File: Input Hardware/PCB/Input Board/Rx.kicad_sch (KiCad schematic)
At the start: 32 parts

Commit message: Update Schematic
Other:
- removed sheet Rx Preamp 5
- removed sheet Rx Preamp 6
- removed sheet Rx Preamp 7
- removed sheet Rx Preamp 8
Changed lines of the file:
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@@
 	)
 	(sheet
-		(at 101.6 73.66)
-		(size 12.7 43.18)
+		(at 203.2 22.86)
+		(size 12.7 93.98)
 		(exclude_from_sim no)
 		(in_bom yes)
@@
 		)
 		(property "Sheetname" "Rx Preamp 4"
-			(at 101.6 72.9484 0)
+			(at 203.2 22.1484 0)
+			(effects
+				(font
+					(size 1.27 1.27)
+				)
+				(justify left bottom)
+			)
+		)
+		(property "Sheetfile" "Rx_Preamp.kicad_sch"
+			(at 203.2 117.4246 0)
+			(effects
+				(font
+					(size 1.27 1.27)
+				)
+				(justify left top)
+			)
+		)
+		(instances
+			(project "Input Board"
+				(path "/198ad8d1-66e3-4deb-889c-1af2b81e67c3/e110e9b7-e557-4981-bab6-c28116ad040e"
+					(page "9")
+				)
+			)
+		)
+	)
+	(sheet
+		(at 152.4 22.86)
+		(size 12.7 93.98)
+		(exclude_from_sim no)
+		(in_bom yes)
+		(on_board yes)
+		(dnp no)
+		(fields_autoplaced yes)
+		(stroke
+			(width 0.1524)
+			(type solid)
+		)
+		(fill
+			(color 0 0 0 0.0000)
+		)
+		(property "Sheetname" "Rx Preamp 3"
+			(at 152.4 22.1484 0)
+			(effects
+				(font
+					(size 1.27 1.27)
+				)
+				(justify left bottom)
+			)
+		)
+		(property "Sheetfile" "Rx_Preamp.kicad_sch"
+			(at 152.4 117.4246 0)
+			(effects
+				(font
+					(size 1.27 1.27)
+				)
+				(justify left top)
+			)
+		)
+		(instances
+			(project "Input Board"
+				(path "/198ad8d1-66e3-4deb-889c-1af2b81e67c3/e110e9b7-e557-4981-bab6-c28116ad040e"
+					(page "7")
+				)
+			)
+		)
+	)
+	(sheet
+		(at 101.6 22.86)
+		(size 12.7 93.98)
+		(exclude_from_sim no)
+		(in_bom yes)
+		(on_board yes)
+		(dnp no)
+		(fields_autoplaced yes)
+		(stroke
+			(width 0.1524)
+			(type solid)
+		)
+		(fill
+			(color 0 0 0 0.0000)
+		)
+		(property "Sheetname" "Rx Preamp 2"
+			(at 101.6 22.1484 0)
 			(effects
 				(font
@@
 			(project "Input Board"
 				(path "/198ad8d1-66e3-4deb-889c-1af2b81e67c3/e110e9b7-e557-4981-bab6-c28116ad040e"
-					(page "6")
-				)
-			)
-		)
-	)
-	(sheet
-		(at 203.2 22.86)
-		(size 12.7 43.18)
-		(exclude_from_sim no)
-		(in_bom yes)
-		(on_board yes)
-		(dnp no)
-		(fields_autoplaced yes)
-		(stroke
-			(width 0.1524)
-			(type solid)
-		)
-		(fill
-			(color 0 0 0 0.0000)
-		)
-		(property "Sheetname" "Rx Preamp 7"
-			(at 203.2 22.1484 0)
-			(effects
-				(font
-					(size 1.27 1.27)
-				)
-				(justify left bottom)
-			)
-		)
-		(property "Sheetfile" "Rx_Preamp.kicad_sch"
-			(at 203.2 66.6246 0)
-			(effects
-				(font
-					(size 1.27 1.27)
-				)
-				(justify left top)
-			)
-		)
-		(instances
-			(project "Input Board"
-				(path "/198ad8d1-66e3-4deb-889c-1af2b81e67c3/e110e9b7-e557-4981-bab6-c28116ad040e"
-					(page "9")
-				)
-			)
-		)
-	)
-	(sheet
-		(at 152.4 22.86)
-		(size 12.7 43.18)
-		(exclude_from_sim no)
-		(in_bom yes)
-		(on_board yes)
-		(dnp no)
-		(fields_autoplaced yes)
-		(stroke
-			(width 0.1524)
-			(type solid)
-		)
-		(fill
-			(color 0 0 0 0.0000)
-		)
-		(property "Sheetname" "Rx Preamp 5"
-			(at 152.4 22.1484 0)
-			(effects
-				(font
-					(size 1.27 1.27)
-				)
-				(justify left bottom)
-			)
-		)
-		(property "Sheetfile" "Rx_Preamp.kicad_sch"
-			(at 152.4 66.6246 0)
-			(effects
-				(font
-					(size 1.27 1.27)
-				)
-				(justify left top)
-			)
-		)
-		(instances
-			(project "Input Board"
-				(path "/198ad8d1-66e3-4deb-889c-1af2b81e67c3/e110e9b7-e557-4981-bab6-c28116ad040e"
-					(page "7")
-				)
-			)
-		)
-	)
-	(sheet
-		(at 101.6 22.86)
-		(size 12.7 43.18)
-		(exclude_from_sim no)
-		(in_bom yes)
-		(on_board yes)
-		(dnp no)
-		(fields_autoplaced yes)
-		(stroke
-			(width 0.1524)
-			(type solid)
-		)
-		(fill
-			(color 0 0 0 0.0000)
-		)
-		(property "Sheetname" "Rx Preamp 3"
-			(at 101.6 22.1484 0)
-			(effects
-				(font
-					(size 1.27 1.27)
-				)
-				(justify left bottom)
-			)
-		)
-		(property "Sheetfile" "Rx_Preamp.kicad_sch"
-			(at 101.6 66.6246 0)
-			(effects
-				(font
-					(size 1.27 1.27)
-				)
-				(justify left top)
-			)
-		)
-		(instances
-			(project "Input Board"
-				(path "/198ad8d1-66e3-4deb-889c-1af2b81e67c3/e110e9b7-e557-4981-bab6-c28116ad040e"
 					(page "5")
 				)
@@
 	)
 	(sheet
-		(at 203.2 73.66)
-		(size 12.7 43.18)
-		(exclude_from_sim no)
-		(in_bom yes)
-		(on_board yes)
-		(dnp no)
-		(fields_autoplaced yes)
-		(stroke
-			(width 0.1524)
-			(type solid)
-		)
-		(fill
-			(color 0 0 0 0.0000)
-		)
-		(property "Sheetname" "Rx Preamp 8"
-			(at 203.2 72.9484 0)
-			(effects
-				(font
-					(size 1.27 1.27)
-				)
-				(justify left bottom)
-			)
-		)
-		(property "Sheetfile" "Rx_Preamp.kicad_sch"
-			(at 203.2 117.4246 0)
-			(effects
-				(font
-					(size 1.27 1.27)
-				)
-				(justify left top)
-			)
-		)
-		(instances
-			(project "Input Board"
-				(path "/198ad8d1-66e3-4deb-889c-1af2b81e67c3/e110e9b7-e557-4981-bab6-c28116ad040e"
-					(page "10")
-				)
-			)
-		)
-	)
-	(sheet
-		(at 50.8 73.66)
-		(size 12.7 43.18)
-		(exclude_from_sim no)
-		(in_bom yes)
-		(on_board yes)
-		(dnp no)
-		(fields_autoplaced yes)
-		(stroke
-			(width 0.1524)
-			(type solid)
-		)
-		(fill
-			(color 0 0 0 0.0000)
-		)
-		(property "Sheetname" "Rx Preamp 2"
-			(at 50.8 72.9484 0)
-			(effects
-				(font
-					(size 1.27 1.27)
-				)
-				(justify left bottom)
-			)
-		)
-		(property "Sheetfile" "Rx_Preamp.kicad_sch"
-			(at 50.8 117.4246 0)
-			(effects
-				(font
-					(size 1.27 1.27)
-				)
-				(justify left top)
-			)
-		)
-		(instances
-			(project "Input Board"
-				(path "/198ad8d1-66e3-4deb-889c-1af2b81e67c3/e110e9b7-e557-4981-bab6-c28116ad040e"
-					(page "4")
-				)
-			)
-		)
-	)
-	(sheet
-		(at 152.4 73.66)
-		(size 12.7 43.18)
-		(exclude_from_sim no)
-		(in_bom yes)
-		(on_board yes)
-		(dnp no)
-		(fields_autoplaced yes)
-		(stroke
-			(width 0.1524)
-			(type solid)
-		)
-		(fill
-			(color 0 0 0 0.0000)
-		)
-		(property "Sheetname" "Rx Preamp 6"
-			(at 152.4 72.9484 0)
-			(effects
-				(font
-					(size 1.27 1.27)
-				)
-				(justify left bottom)
-			)
-		)
-		(property "Sheetfile" "Rx_Preamp.kicad_sch"
-			(at 152.4 117.4246 0)
-			(effects
-				(font
-					(size 1.27 1.27)
-				)
-				(justify left top)
-			)
-		)
-		(instances
-			(project "Input Board"
-				(path "/198ad8d1-66e3-4deb-889c-1af2b81e67c3/e110e9b7-e557-4981-bab6-c28116ad040e"
-					(page "8")
-				)
-			)
-		)
-	)
-	(sheet
-		(at 50.8 22.86)
-		(size 12.7 43.18)
+		(at 50.8 24.13)
+		(size 12.7 92.71)
 		(exclude_from_sim no)
 		(in_bom yes)
@@
 		)
 		(property "Sheetname" "Rx Preamp  1"
-			(at 50.8 22.1484 0)
+			(at 50.8 23.4184 0)
 			(effects
 				(font
@@
 		)
 		(property "Sheetfile" "Rx_Preamp.kicad_sch"
-			(at 50.8 66.6246 0)
+			(at 50.8 117.4246 0)
 			(effects
 				(font

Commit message: Fix Name
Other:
- sheet Rx Preamp  1 renamed Rx Preamp 1
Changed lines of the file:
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@@
 			(color 0 0 0 0.0000)
 		)
-		(property "Sheetname" "Rx Preamp  1"
+		(property "Sheetname" "Rx Preamp 1"
 			(at 50.8 23.4184 0)
 			(effects

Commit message: Power Board, Row amplifier setup etc
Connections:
- net Rx Row Amplifier 1/RXIN5: now reaches L205.2
- net Rx Row Amplifier 1/RXIN6: now reaches L206.2
- net Rx Row Amplifier 1/RXIN4: now reaches L204.2
- net Rx Row Amplifier 1/RXIN8: now reaches L208.2
- net Rx Row Amplifier 1/RXIN7: now reaches L207.2
- net Rx Row Amplifier 1/RXIN2: now reaches L202.2
- net Rx Row Amplifier 1/RXIN1: now reaches L201.2
- net Rx Row Amplifier 1/RXIN3: now reaches L203.2
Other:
- sheet Rx Preamp 1 renamed Rx Row Amplifier 1
- sheet Rx Preamp 2 renamed Rx Row Amplifier 2
- sheet Rx Preamp 3 renamed Rx Row Amplifier 3
- sheet Rx Preamp 4 renamed Rx Row Amplifier 4
- sheet Rx Row Amplifier 1 ports: added RXIN1, RXIN2, RXIN3, RXIN4, RXIN5, RXIN6, RXIN7, RXIN8, RXOUT1, RXOUT2, RXOUT3, RXOUT4, RXOUT5, RXOUT6, RXOUT7, RXOUT8; removed none
- moved on the sheet: L201, L202, L203, L204, L205, L206, L207, L208, L209, L210, L211, L212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

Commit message: explosion 💥
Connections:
- net Rx Row Amplifier 4/RXIN4: now reaches L228.2
- net Rx Row Amplifier 2/RXOUT4: now reaches L212.2
- net Rx Row Amplifier 4/RXIN6: now reaches L230.2
- net Rx Row Amplifier 2/RXIN8: now reaches L213.2
- net Rx Row Amplifier 3/RXIN3: now reaches L219.2
- net Rx Row Amplifier 3/RXIN1: now reaches L217.2
- net Rx Row Amplifier 4/RXIN7: now reaches L231.2
- net Rx Row Amplifier 2/RXOUT2: now reaches L210.2
- net Rx Row Amplifier 2/RXIN1: now reaches L209.2
- net Rx Row Amplifier 4/RXIN5: now reaches L229.2
- net Rx Row Amplifier 4/RXIN1: now reaches L225.2
- net Rx Row Amplifier 3/RXIN5: now reaches L221.2
- net Rx Row Amplifier 3/RXIN7: now reaches L223.2
- net Rx Row Amplifier 4/RXIN3: now reaches L227.2
- net Rx Row Amplifier 4/RXIN8: now reaches L232.2
- net Rx Row Amplifier 3/RXOUT4: now reaches L220.2
- net Rx Row Amplifier 2/RXIN7: now reaches L214.2
- net Rx Row Amplifier 2/RXOUT7: now reaches L216.2
- net Rx Row Amplifier 3/RXIN6: now reaches L222.2
- net Rx Row Amplifier 3/RXOUT2: now reaches L218.2
- net Rx Row Amplifier 3/RXIN8: now reaches L224.2
- net Rx Row Amplifier 2/RXIN5: now reaches L215.2
- net Rx Row Amplifier 2/RXIN3: now reaches L211.2
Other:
- sheet Rx Row Amplifier 2 ports: added RXIN1, RXIN2, RXIN3, RXIN4, RXIN5, RXIN6, RXIN7, RXIN8, RXOUT1, RXOUT2, RXOUT3, RXOUT4, RXOUT5, RXOUT6, RXOUT7, RXOUT8; removed none
- sheet Rx Row Amplifier 3 ports: added RXIN1, RXIN2, RXIN3, RXIN4, RXIN5, RXIN6, RXIN7, RXIN8, RXOUT1, RXOUT2, RXOUT3, RXOUT4, RXOUT5, RXOUT6, RXOUT7, RXOUT8; removed none
- sheet Rx Row Amplifier 4 ports: added RXIN1, RXIN2, RXIN3, RXIN4, RXIN5, RXIN6, RXIN7, RXIN8, RXOUT1, RXOUT2, RXOUT3, RXOUT4, RXOUT5, RXOUT6, RXOUT7, RXOUT8; removed none
- moved on the sheet: L209, L210, L211, L212, L213, L214, L215, L216, L217, L218, L219, L220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

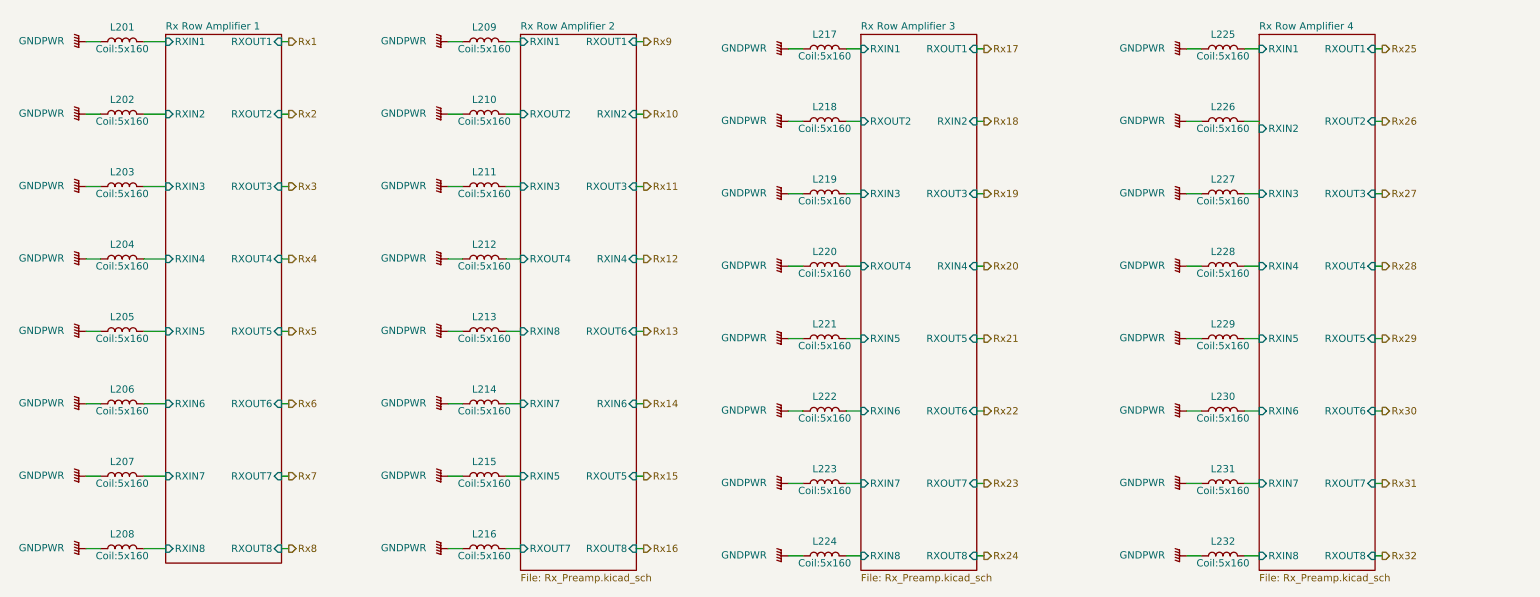
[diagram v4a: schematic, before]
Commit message: row amp fixes and spice fixes
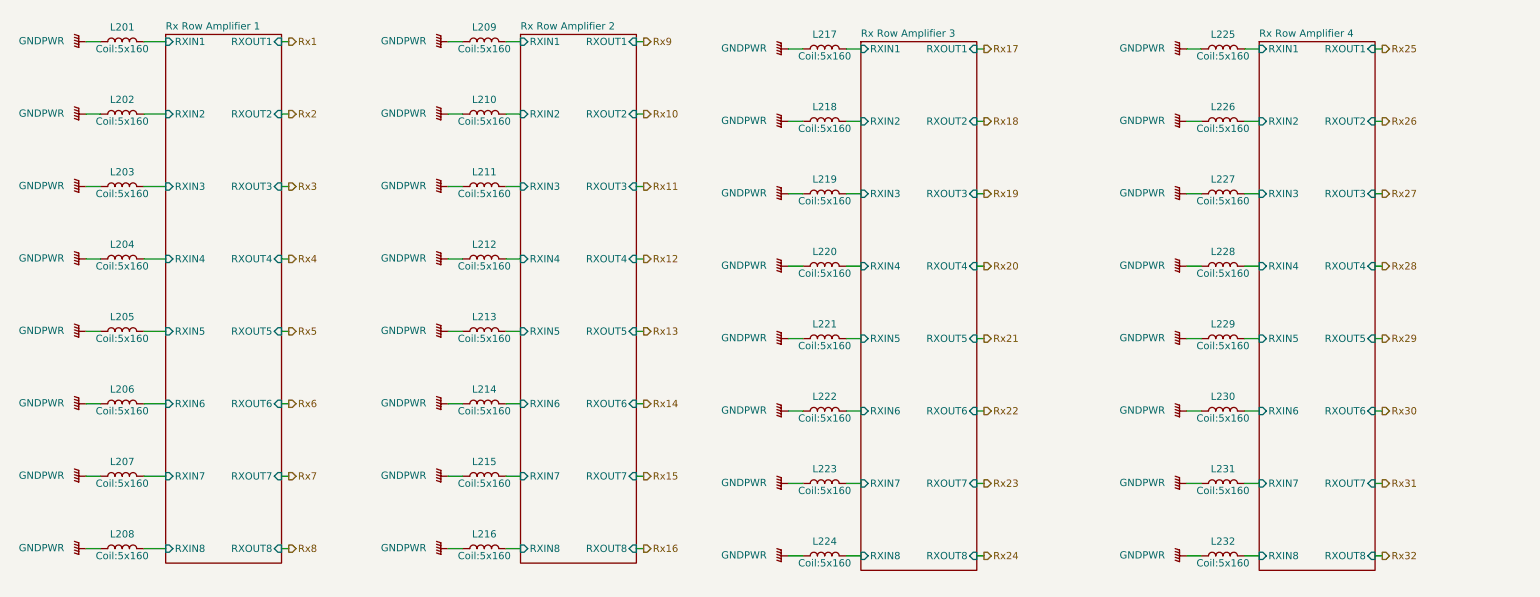
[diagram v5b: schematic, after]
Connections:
- net Rx Row Amplifier 2/RXOUT7 is gone; now on net Rx Row Amplifier 2/RXIN8: L216.2
- net Rx Row Amplifier 2/RXIN5: now also L213.2; no longer L215.2
- net Rx Row Amplifier 2/RXIN7: now also L215.2; no longer L214.2
- net Rx Row Amplifier 2/RXIN8: no longer L213.2
- net Rx Row Amplifier 4/RXIN2: now also L226.2
- net Rx Row Amplifier 2/RXOUT2 renamed Rx Row Amplifier 2/RXIN2
- net Rx Row Amplifier 2/RXOUT4 renamed Rx Row Amplifier 2/RXIN4
- net Rx Row Amplifier 3/RXOUT2 renamed Rx Row Amplifier 3/RXIN2
- net Rx Row Amplifier 3/RXOUT4 renamed Rx Row Amplifier 3/RXIN4
- new net Rx Row Amplifier 2/RXIN6: L214.2

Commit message: Layout
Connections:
- net GNDPWR renamed GND

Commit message: Change topology
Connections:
- net Rx Row Amplifier 1/RXIN1 is gone; now on net Rx1: L201.2
- net Rx Row Amplifier 1/RXIN2 is gone; now on net Rx2: L202.2
- net Rx Row Amplifier 1/RXIN3 is gone; now on net Rx3: L203.2
- net Rx Row Amplifier 1/RXIN4 is gone; now on net Rx4: L204.2
- net Rx Row Amplifier 1/RXIN5 is gone; now on net Rx5: L205.2
- net Rx Row Amplifier 1/RXIN6 is gone; now on net Rx6: L206.2
- net Rx Row Amplifier 1/RXIN7 is gone; now on net Rx7: L207.2
- net Rx Row Amplifier 1/RXIN8 is gone; now on net Rx8: L208.2
- net Rx Row Amplifier 2/RXIN1 is gone; now on net Rx9: L209.2
- net Rx Row Amplifier 2/RXIN2 is gone; now on net Rx10: L210.2
- net Rx Row Amplifier 2/RXIN3 is gone; now on net Rx11: L211.2
- net Rx Row Amplifier 2/RXIN4 is gone; now on net Rx12: L212.2
- net Rx Row Amplifier 2/RXIN5 is gone; now on net Rx13: L213.2
- net Rx Row Amplifier 2/RXIN6 is gone; now on net Rx14: L214.2
- net Rx Row Amplifier 2/RXIN7 is gone; now on net Rx15: L215.2
- net Rx Row Amplifier 2/RXIN8 is gone; now on net Rx16: L216.2
- net Rx Row Amplifier 3/RXIN1 is gone; now on net Rx17: L217.2
- net Rx Row Amplifier 3/RXIN2 is gone; now on net Rx18: L218.2
- net Rx Row Amplifier 3/RXIN3 is gone; now on net Rx19: L219.2
- net Rx Row Amplifier 3/RXIN4 is gone; now on net Rx20: L220.2
- net Rx Row Amplifier 3/RXIN5 is gone; now on net Rx21: L221.2
- net Rx Row Amplifier 3/RXIN6 is gone; now on net Rx22: L222.2
- net Rx Row Amplifier 3/RXIN7 is gone; now on net Rx23: L223.2
- net Rx Row Amplifier 3/RXIN8 is gone; now on net Rx24: L224.2
- net Rx Row Amplifier 4/RXIN1 is gone; now on net Rx25: L225.2
- net Rx Row Amplifier 4/RXIN2 is gone; now on net Rx26: L226.2
- net Rx Row Amplifier 4/RXIN3 is gone; now on net Rx27: L227.2
- net Rx Row Amplifier 4/RXIN4 is gone; now on net Rx28: L228.2
- net Rx Row Amplifier 4/RXIN5 is gone; now on net Rx29: L229.2
- net Rx Row Amplifier 4/RXIN6 is gone; now on net Rx30: L230.2
- net Rx Row Amplifier 4/RXIN7 is gone; now on net Rx31: L231.2
- net Rx Row Amplifier 4/RXIN8 is gone; now on net Rx32: L232.2
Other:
- removed sheet Rx Row Amplifier 1
- removed sheet Rx Row Amplifier 2
- removed sheet Rx Row Amplifier 3
- removed sheet Rx Row Amplifier 4
